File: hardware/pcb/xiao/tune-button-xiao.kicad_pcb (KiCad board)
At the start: 2 copper layers, 46 x 64.5 mm, 18 parts, among them J1 XIAO left, J2 XIAO right, J3 LiPo, J4 to XIAO BAT, SW1 MX switch, SW2 MX switch, SW3 MX switch, SW4 MX switch

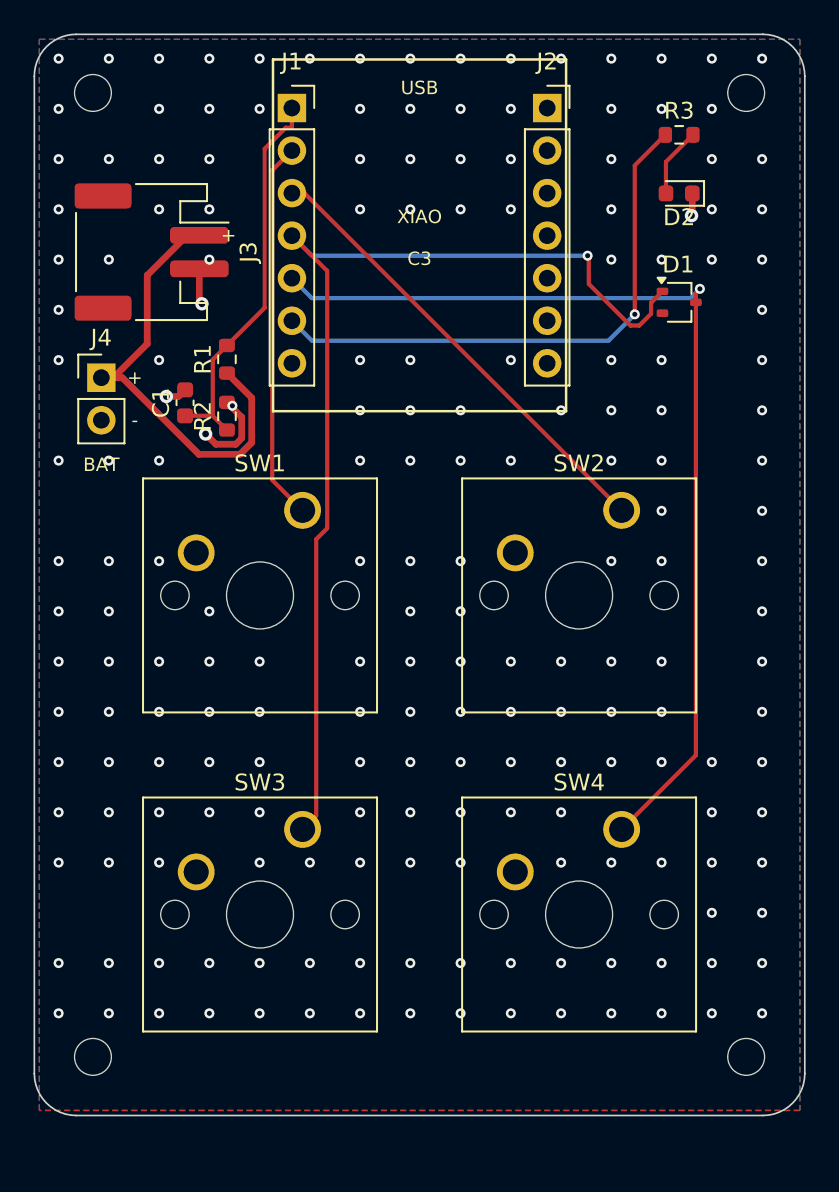
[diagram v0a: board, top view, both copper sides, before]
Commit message: PCBs: keep screw heads and labels clear of the keycaps
Mounting holes move out from under the caps (both boards 2.5 mm longer), and part labels are placed
automatically beside each part, off pads, bodies and the XIAO's outline.
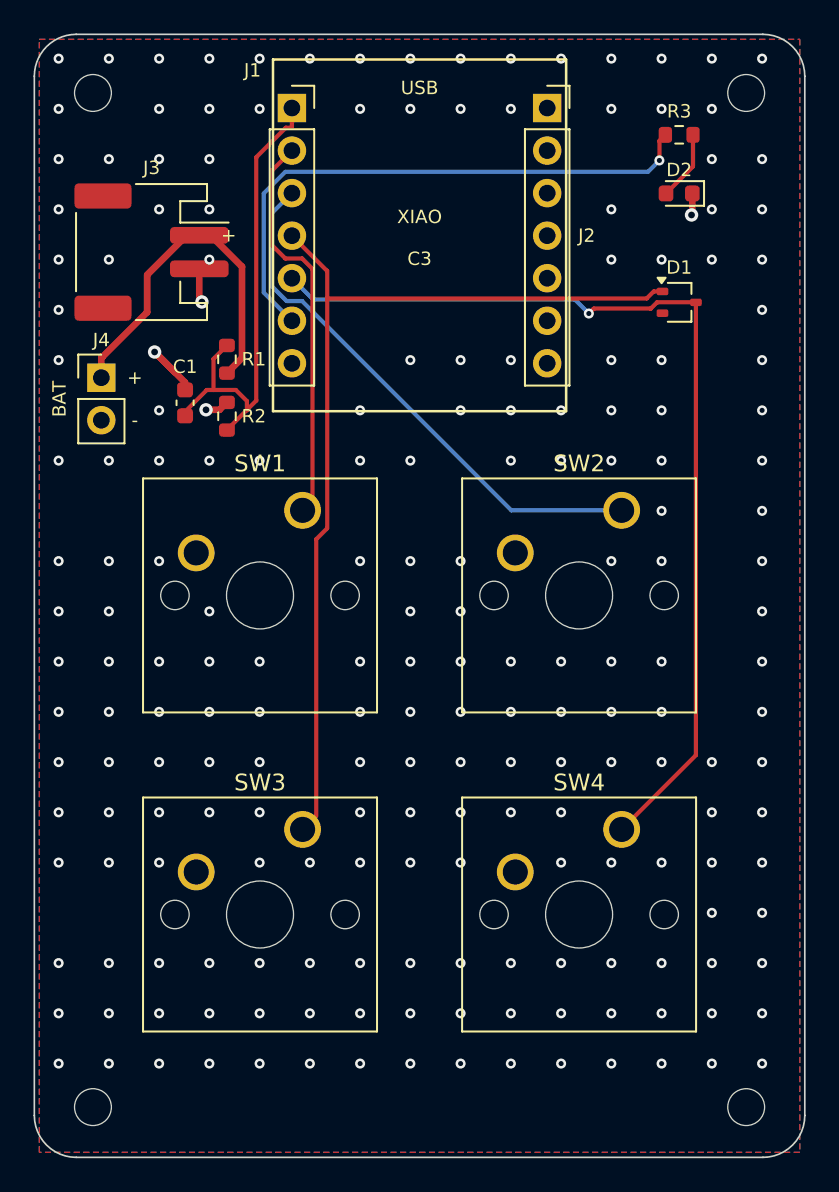
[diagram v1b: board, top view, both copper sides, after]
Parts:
- moved H3 3.00 mm to (3.50, 64.0)
- moved H4 3.00 mm to (42.5, 64.0)
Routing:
- net K3: track 63.6 -> 57.1 mm, vias 1 -> 0
- net VBAT_SENSE: track 23.4 -> 29.3 mm
- net VBAT: track 27.0 -> 21.5 mm
- net K2: track 27.5 -> 32.5 mm
- net LED: track 33.1 -> 34.4 mm
- net K1: track 22.7 -> 23.8 mm
- net K4: track 59.3 -> 58.6 mm
- net GND: track 10.7 -> 11.2 mm, vias 200 -> 207
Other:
- board size 46 x 64.5 mm -> 46 x 67 mm

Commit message: C3 PCB: no board under the antenna, USB-C to the bottom edge
The top-left corner is cut away under the module's antenna, as Espressif's layout guide prefers,
and USB-C moves to the middle of the bottom edge (about 70 mm from the antenna) with its ESD
part and CC resistors between the lower switches. The receptacle's face now sits 0.2 mm proud of
the edge so a plug's moulding clears the board.
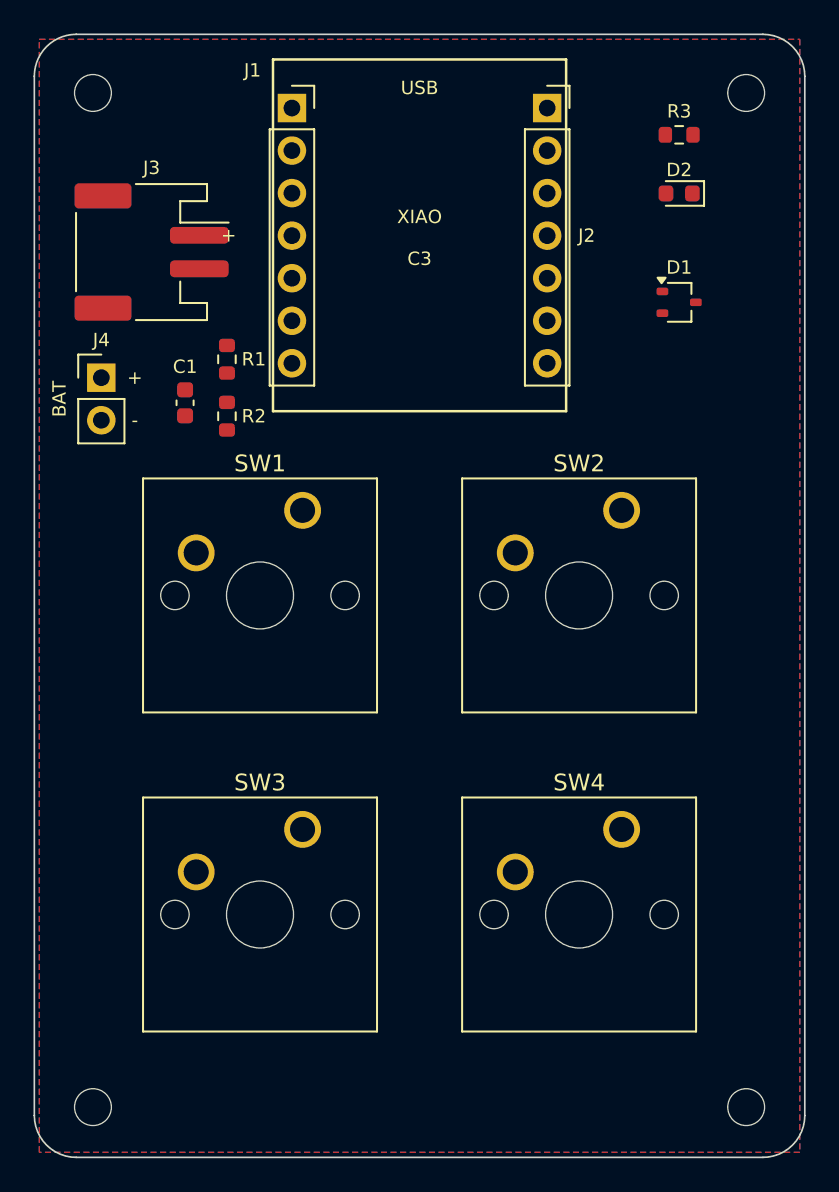
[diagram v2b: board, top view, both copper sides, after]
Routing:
- net K4: track 58.6 -> 0.00 mm, vias 1 -> 0
- net K3: track 57.1 -> 0.00 mm
- net LED: track 34.4 -> 0.00 mm, vias 1 -> 0
- net K2: track 32.5 -> 0.00 mm
- net VBAT_SENSE: track 29.3 -> 0.00 mm
- net K1: track 23.8 -> 0.00 mm
- net VBAT: track 21.5 -> 0.00 mm
- net GND: track 11.2 -> 0.00 mm, vias 207 -> 0
- net LED_A: track 4.17 -> 0.00 mm

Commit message: C3 PCB: JLC Basic/Preferred parts where a drop-in exists, LCSC numbers, JLC BOM and CPL
TP4054 for MCP73831, XC6206 for MCP1700 and SRV05-4 for USBLC6-2SC6, each with the same footprint
and pinout. Every assembled part carries its LCSC number; the build writes JLC-format BOM and
placement files listing only those parts. Only the module, USB-C and JST sockets remain Extended.
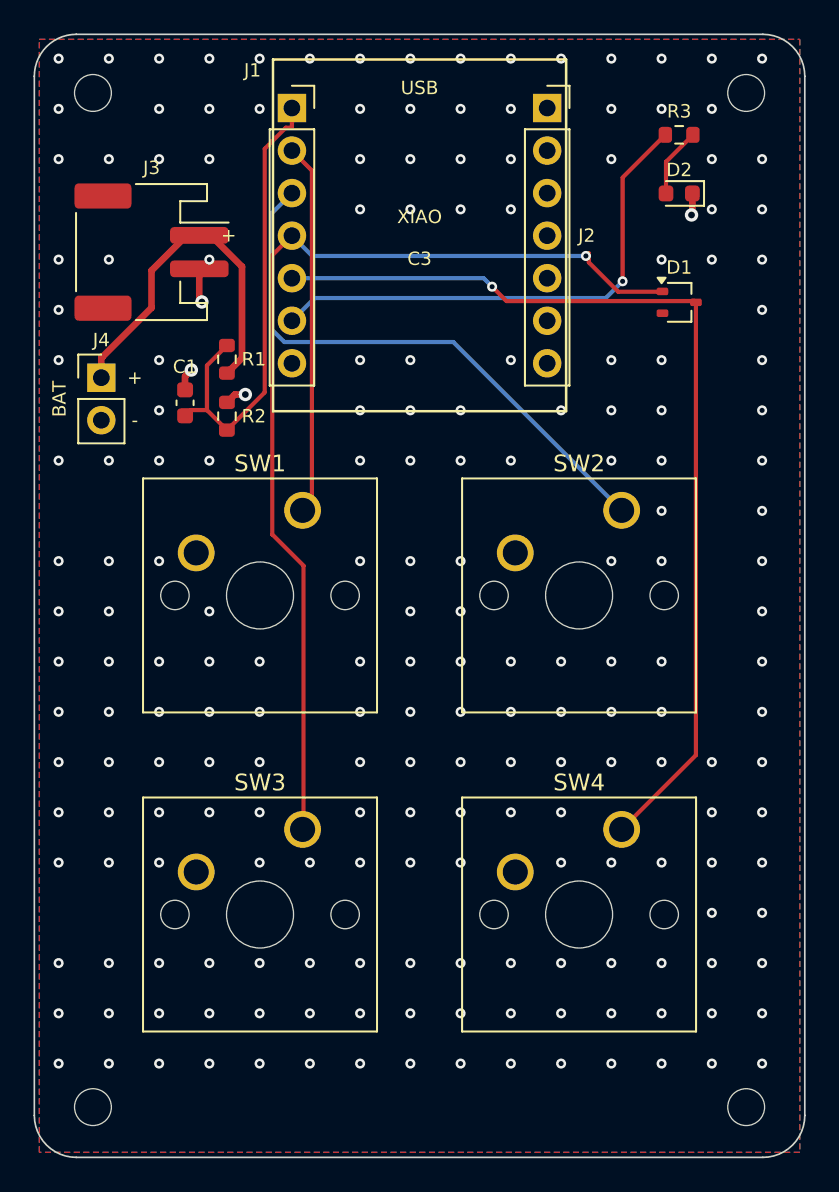
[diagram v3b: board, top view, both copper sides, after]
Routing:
- net K3: track 0.00 -> 60.7 mm, vias 0 -> 1
- net K4: track 0.00 -> 58.0 mm, vias 0 -> 1
- net K2: track 0.00 -> 34.0 mm
- net LED: track 0.00 -> 30.5 mm, vias 0 -> 1
- net VBAT_SENSE: track 0.00 -> 28.6 mm
- net K1: track 0.00 -> 22.2 mm
- net VBAT: track 0.00 -> 21.5 mm
- net GND: track 0.00 -> 5.98 mm, vias 0 -> 211
- net LED_A: track 0.00 -> 4.17 mm

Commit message: C3 PCB: switches and LEDs on the back, electronics on the front, EdgeCoil mark on the key side
The MX switches mount on the back (mirrored so K1 is still top left from the key side), and only
their leads and posts need room on the front, guarded by part-free rule areas. That lets the keys
sit behind the electronics: the board is 69.5 mm long instead of 80.5. The two LEDs move to the key
side as hand-soldered 0805s; the battery socket and UART pads sit between the key rows. The key side
carries the mark, the board name and LED labels; part labels are placed per side and kept off the
antenna notch.
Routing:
- net K2: track 34.0 -> 27.5 mm
- net K3: track 60.7 -> 62.6 mm
- net K4: track 58.0 -> 59.9 mm
- net GND: track 5.98 -> 7.57 mm, vias 211 -> 215
- net K1: track 22.2 -> 22.7 mm
- net LED: track 30.5 -> 31.0 mm

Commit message: pcb: MCP1700 regulator, edgecoil.dev on the silkscreen, mark under its own licence
The EdgeCoil mark, name and URL are all rights reserved and outside CERN-OHL-S; derivatives must
remove them. The C3 board's regulator goes back to the 250 mA MCP1700 (C39051, Extended).
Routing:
- net K2: track 27.5 -> 32.5 mm
- net VBAT_SENSE: track 29.0 -> 24.6 mm
- net VBAT: track 21.4 -> 17.2 mm
- net LED: track 31.0 -> 26.9 mm, vias 1 -> 0
- net K4: track 59.9 -> 58.0 mm
- net K1: track 22.7 -> 24.2 mm
- net K3: track 62.6 -> 61.2 mm
- net GND: track 7.57 -> 6.48 mm, vias 215 -> 207
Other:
- board text added: "tune-button xiao edgecoil.dev rev A"
- board text removed: "tune-button xiao edgecoil rev A"

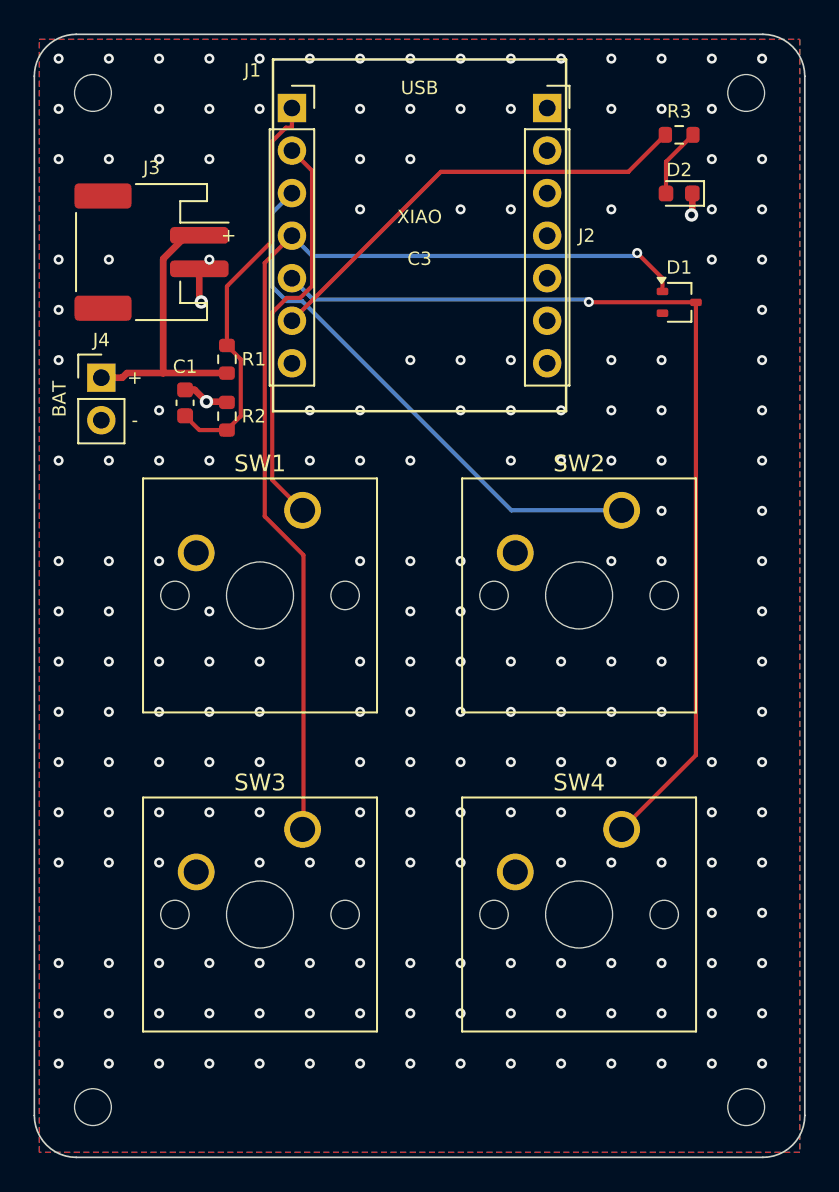
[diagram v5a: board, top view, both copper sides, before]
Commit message: pcb: DFM fixes from audit; artwork clear of drilled holes
- fab_jlc.py: per-part CPL rotation and origin corrections (MCP1700, AO3401A, SRV05-4, TP4054,
  USB-C), checked against JLC's own footprints; the SRV05-4 one would have shorted VBUS.
- Paste on the USB-C shell slots; thermal spokes on all pour pads; copper 0.3 mm from the edge.
- Silkscreen text 1.0 mm / 0.15 mm; switch-pin keep-outs 2.5 mm, R10/R11/C7 moved for iron room.
- Via-free rule areas under back artwork, honoured by the stitcher; the build refuses a footprint
  hole under artwork. C3 mark moved off the module's ground vias; XIAO text off SW4's pins.
- No drill maps or back paste in the gerber zip.
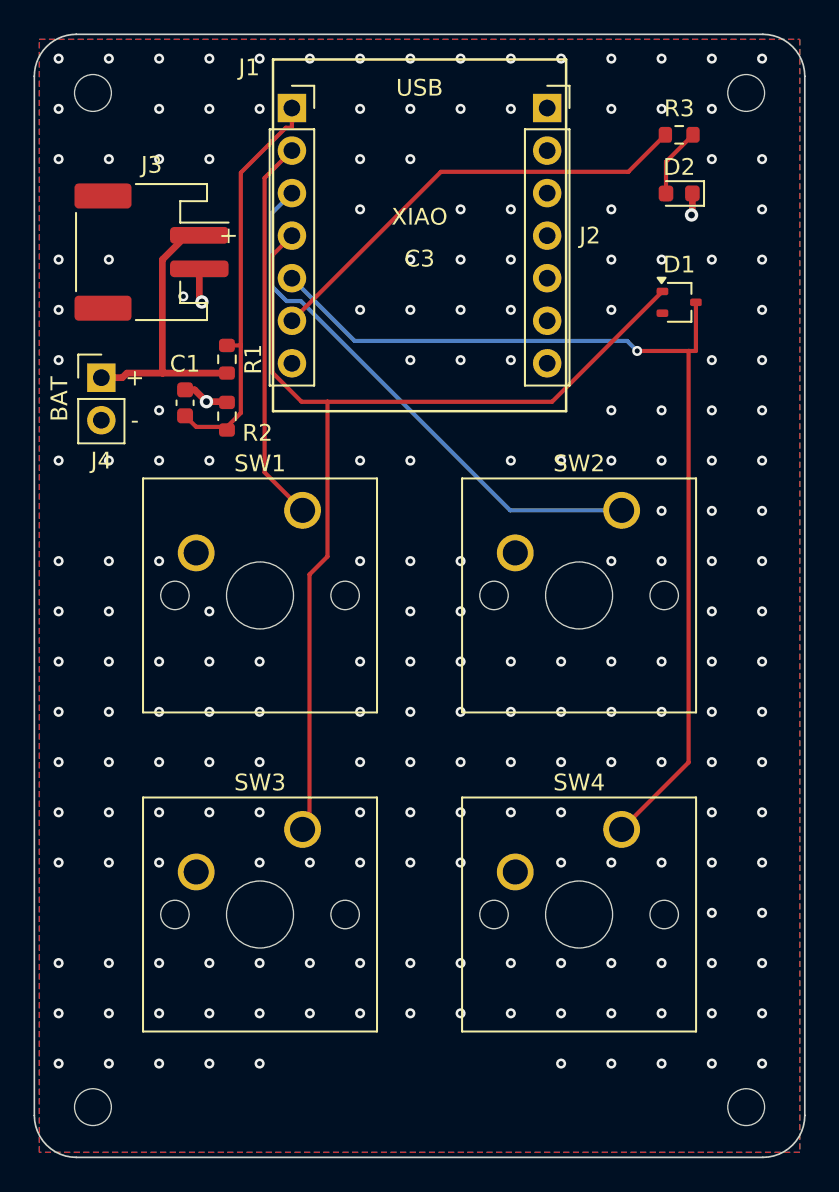
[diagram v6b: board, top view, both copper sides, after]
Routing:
- net K1: track 24.2 -> 23.1 mm
- net K4: track 58.0 -> 59.0 mm
- net K3: track 61.2 -> 61.6 mm, vias 1 -> 0
- net GND: track 6.48 -> 6.16 mm, vias 207 -> 211

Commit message: pcb (c3): power-path fixes from simulation
- SRV05-4 rail on 3V3, not VBUS: on battery the D+ pull-up leaked onto VBUS (2.6 V simulated)
  and half turned off the battery FET.
- 1 ohm in series with the charger's input capacitor: plug-in ringing peaked near 7 V, past the
  regulator's 6.5 V limit.
- R5 100k -> 10k: Q1 turns back on ~3 ms after unplugging rather than ~15 ms, and stays on
  against D2's leakage when warm.
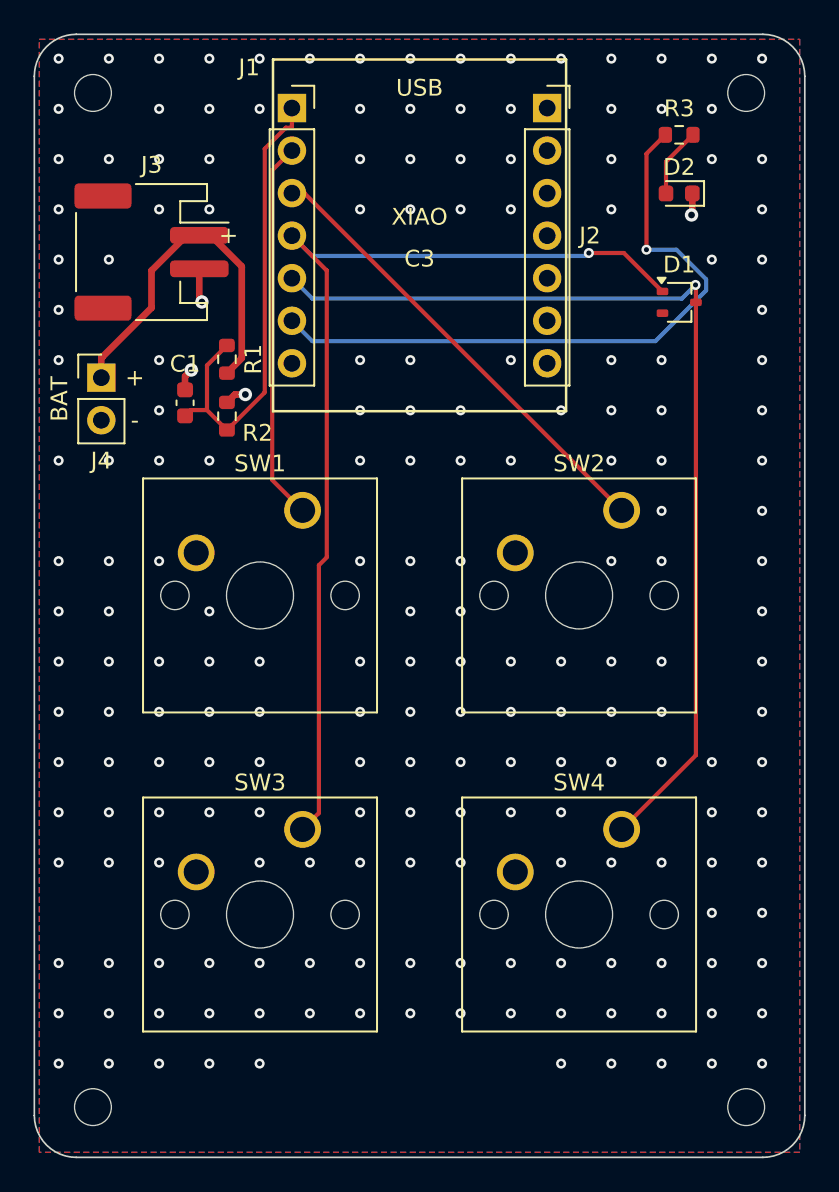
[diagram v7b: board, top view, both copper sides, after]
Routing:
- net LED: track 26.9 -> 38.8 mm, vias 0 -> 1
- net K2: track 32.5 -> 27.5 mm
- net VBAT: track 17.2 -> 21.4 mm
- net VBAT_SENSE: track 24.7 -> 28.6 mm
- net K3: track 61.6 -> 60.6 mm, vias 0 -> 1
- net GND: track 6.16 -> 6.42 mm, vias 211 -> 207

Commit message: pcb (c3): RT9080 600 mA regulator
Covers Wi-Fi's ~350 mA transmit peaks (current limit >= 610 mA, 2 uA quiescent); SOT-23-5 with the
AP2112K symbol's pinout, EN tied on. JLC CPL rotation +270, from JLC's own footprint.
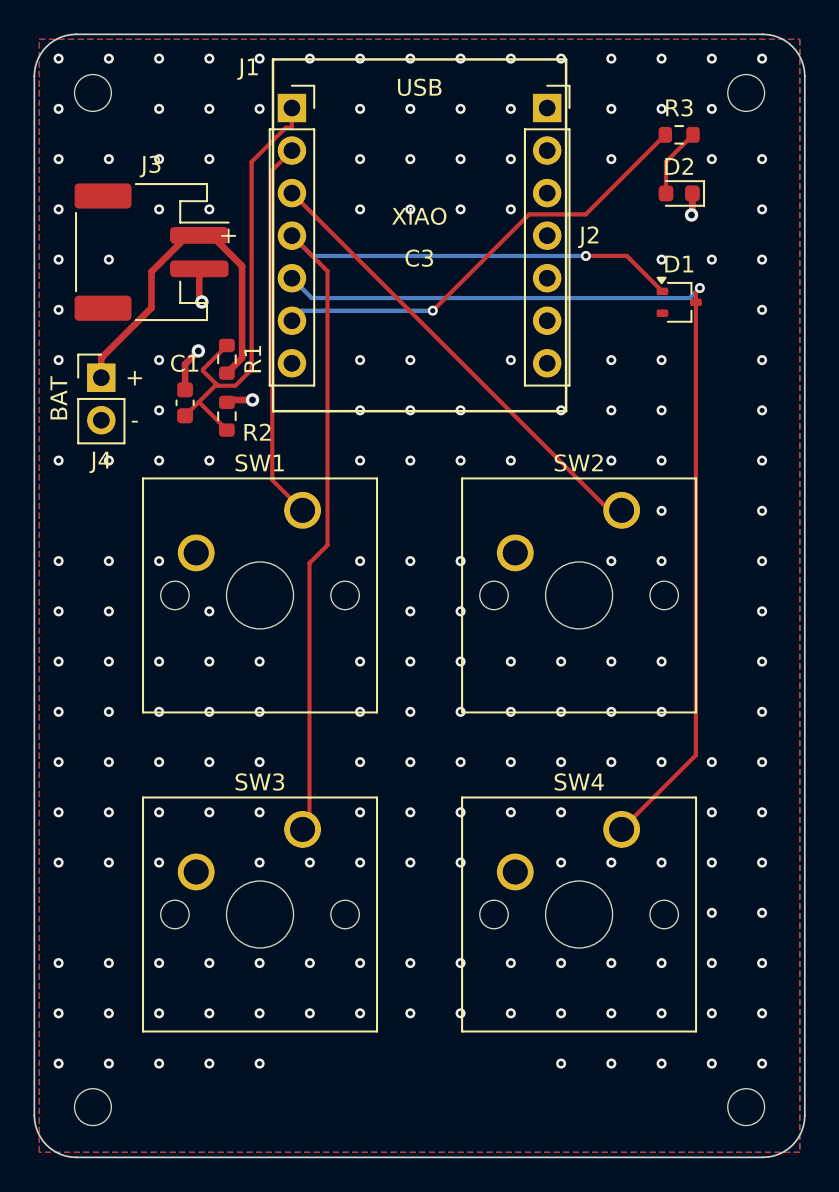
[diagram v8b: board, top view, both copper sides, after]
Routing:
- net LED: track 38.8 -> 26.9 mm
- net GND: track 6.42 -> 7.59 mm
- net VBAT_SENSE: track 28.6 -> 27.6 mm
